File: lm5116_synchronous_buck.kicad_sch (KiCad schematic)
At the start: 60 parts

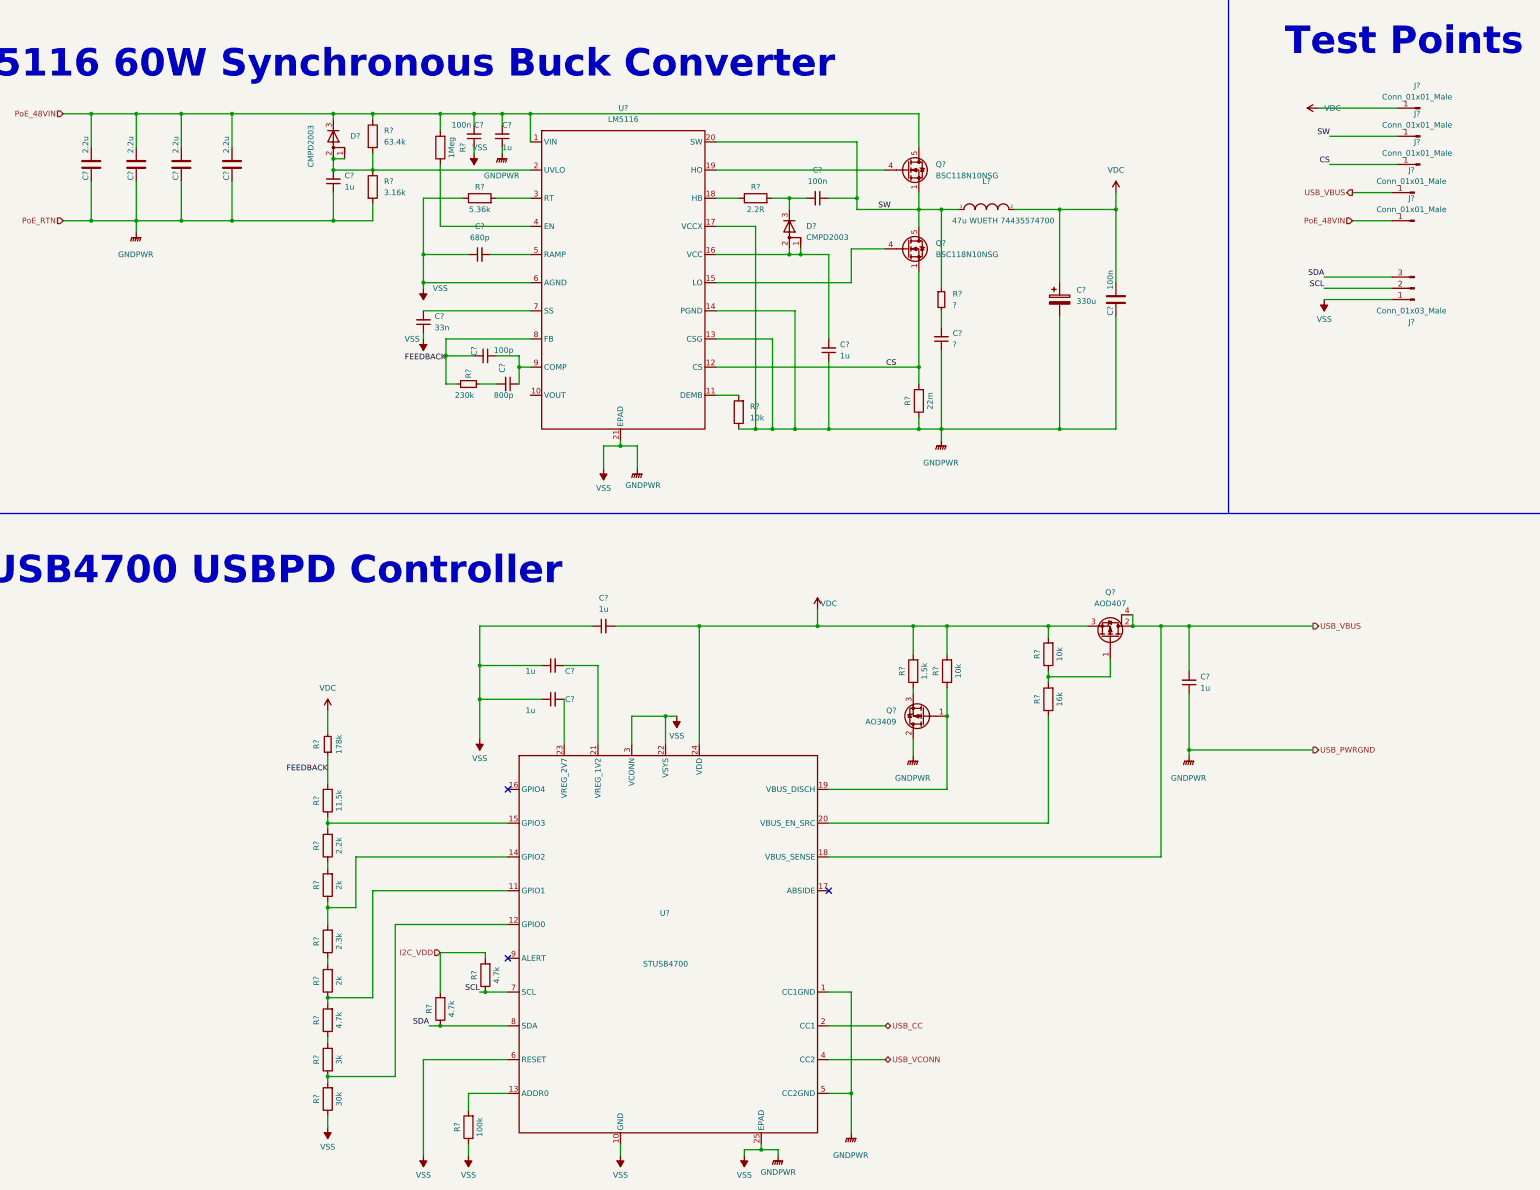
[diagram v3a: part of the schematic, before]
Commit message: finished lm5116 circuit foot print assignment
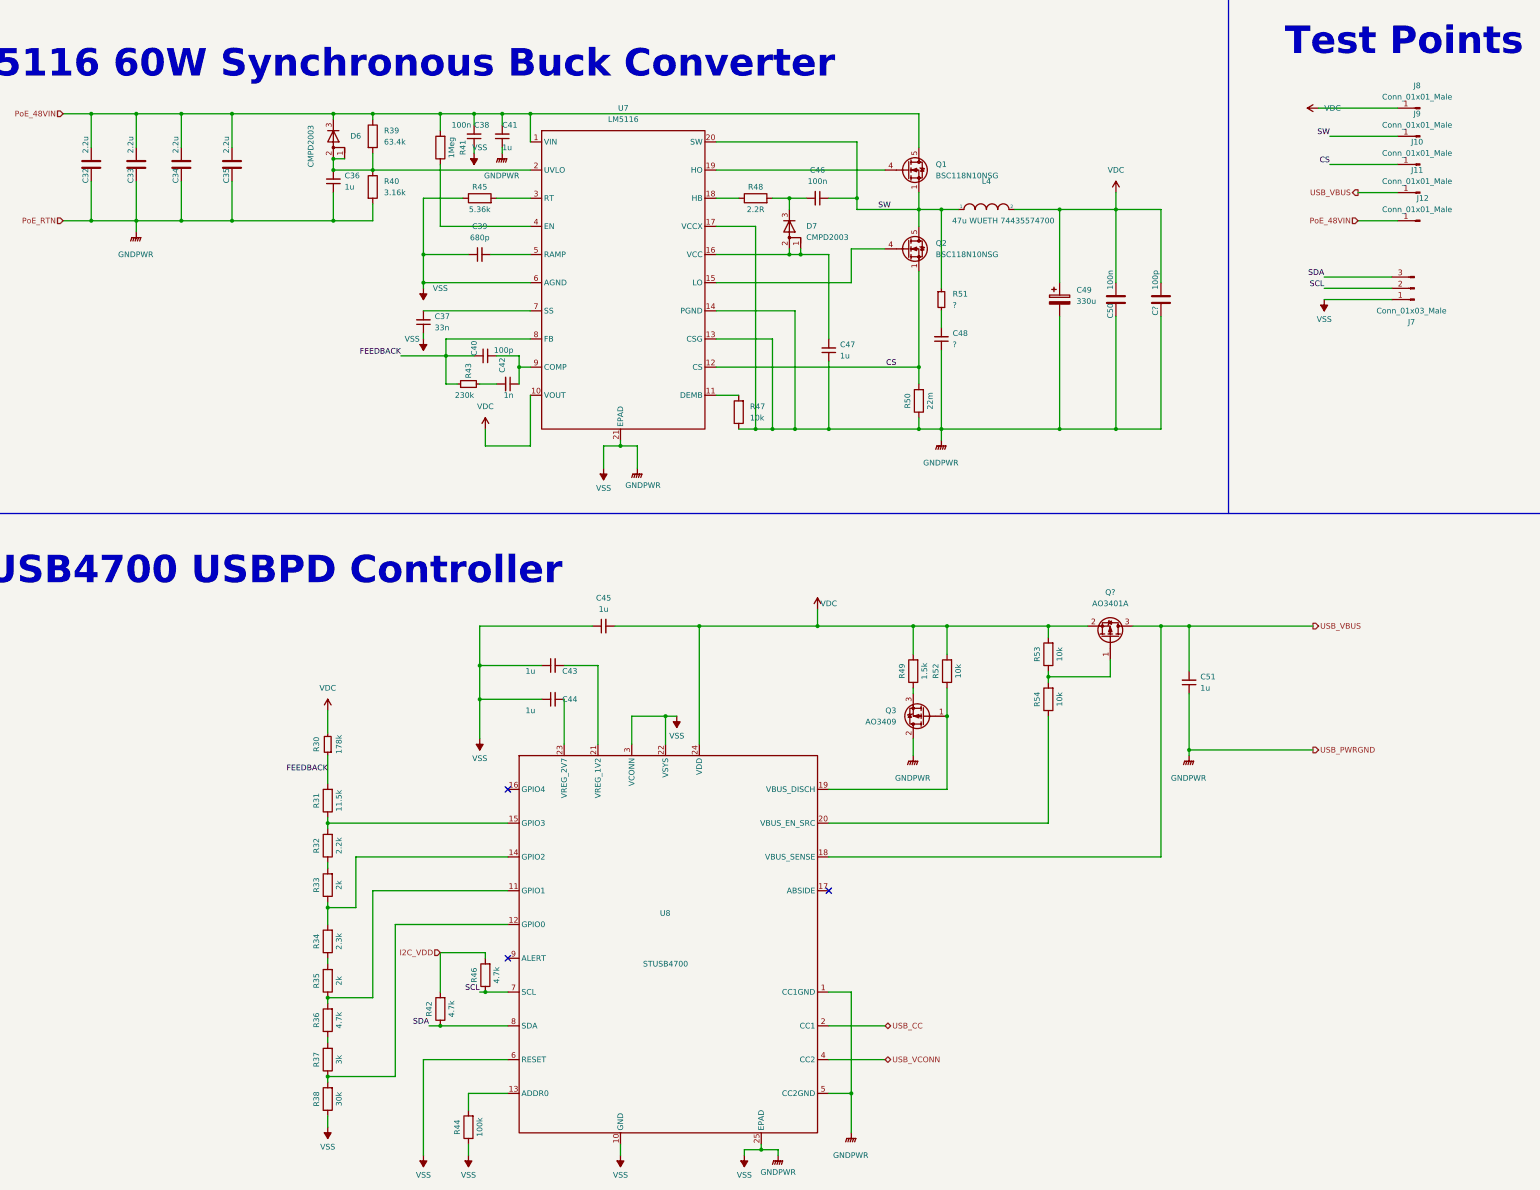
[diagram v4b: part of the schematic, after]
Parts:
- removed Q?: AOD407, symbol Device:Q_PMOS_GDSD
- added C?: 100p, Capacitor_SMD:C_0603_1608Metric, symbol Device:C
- added Q?: AO3401A, Package_TO_SOT_SMD:SOT-23, symbol Transistor_FET:AO3401A
- C32, C33, C34, C35, C36, C37, C38, C39, C40, C41, C43, C44, C45, C46, C47, C48, C50: renamed from C?; footprint (none) -> Capacitor_SMD:C_0603_1608Metric
- C42: renamed from C?; value 800p -> 1n; footprint (none) -> Capacitor_SMD:C_0603_1608Metric
- D6, D7: renamed from D?; footprint (none) -> Package_TO_SOT_SMD:SOT-23
- J10, J11, J12, J8, J9: renamed from J?; footprint (none) -> Connector_PinHeader_1.00mm:PinHeader_1x01_P1.00mm_Vertical
- J7: renamed from J?; footprint (none) -> Connector_PinHeader_1.00mm:PinHeader_1x03_P1.00mm_Vertical
- Q3: renamed from Q?; footprint (none) -> Package_TO_SOT_SMD:SOT-23
- R30, R31, R32, R33, R34, R35, R36, R37, R38, R40, R41, R42, R43, R44, R45, R46, R47, R49, R51, R52, R53: renamed from R?; footprint (none) -> Resistor_SMD:R_0603_1608Metric
- R48: renamed from R?; footprint (none) -> Resistor_SMD:R_0805_2012Metric
- R50: renamed from R?; footprint (none) -> Resistor_SMD:R_1206_3216Metric
- R54: renamed from R?; value 16k -> 10k; footprint (none) -> Resistor_SMD:R_0603_1608Metric
- gave numbers to parts that had none: 8
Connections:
- net GNDPWR: now also C?.2
- net USB_VBUS: now also Q?.3 (D)
- net VDC: now also U7.10 (VOUT), C?.1, Q?.2 (S)
- net at R53.1, R54.2: now also Q?.1 (G)
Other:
- moved on the sheet: J11, J12

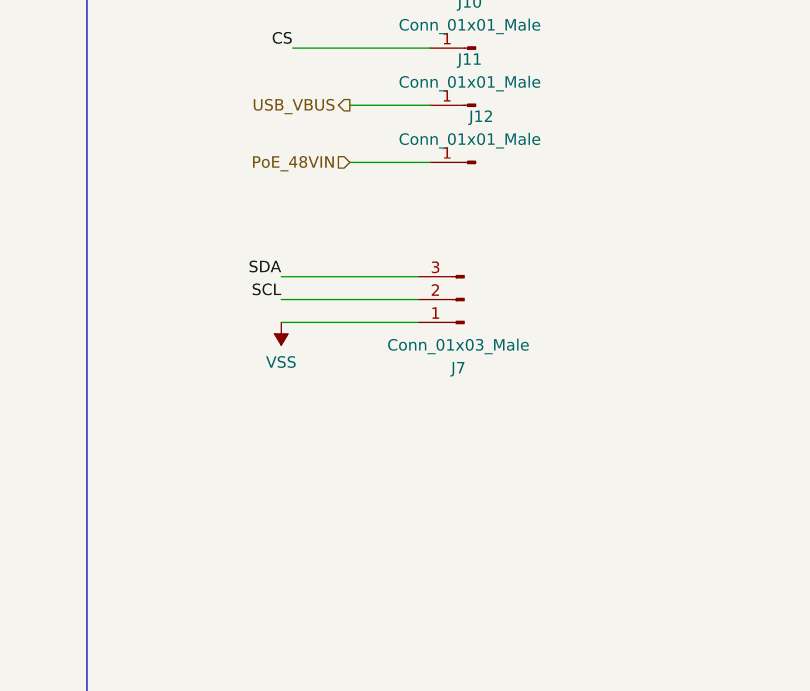
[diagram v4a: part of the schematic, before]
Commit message: footprint for power inductor and cap
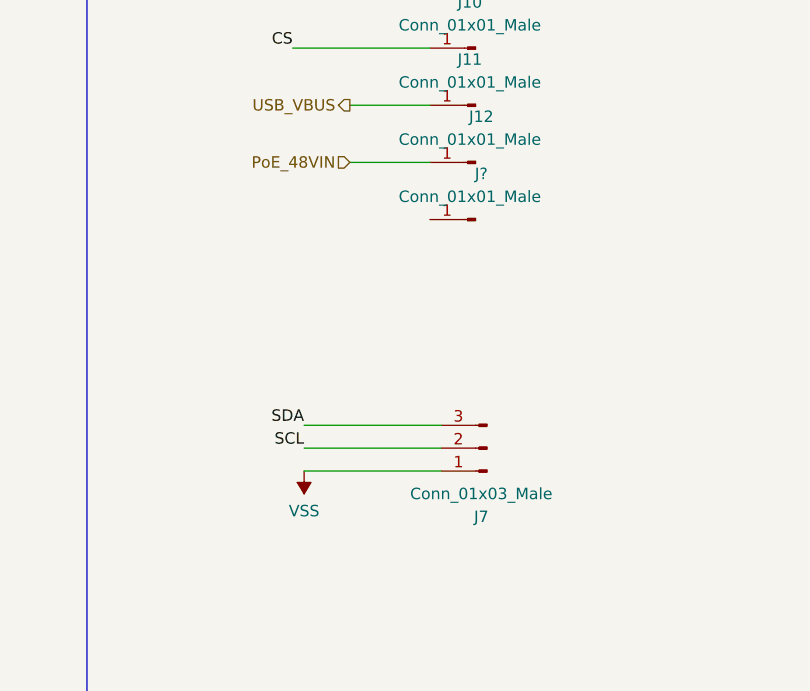
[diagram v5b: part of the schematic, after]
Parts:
- added J?: Conn_01x01_Male, Connector_PinHeader_1.00mm:PinHeader_1x01_P1.00mm_Vertical, symbol Connector:Conn_01x01_Male
- C49: footprint (none) -> Capacitor_SMD:C_Elec_10x10.2
- L4: footprint (none) -> PoE_Devices:74435574700
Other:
- moved on the sheet: J7
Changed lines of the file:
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@@
     (stroke (width 0) (type default) (color 0 0 0 0))
   )
-  (wire (pts (xy 331.47 82.55) (xy 346.71 82.55))
+  (wire (pts (xy 334.01 99.06) (xy 349.25 99.06))
     (stroke (width 0) (type default) (color 0 0 0 0))
   )
@@
     (stroke (width 0) (type default) (color 0 0 0 0))
   )
-  (wire (pts (xy 331.47 80.01) (xy 346.71 80.01))
+  (wire (pts (xy 334.01 96.52) (xy 349.25 96.52))
     (stroke (width 0) (type default) (color 0 0 0 0))
   )
@@
     (stroke (width 0) (type default) (color 0 0 0 0))
   )
-  (wire (pts (xy 331.47 77.47) (xy 346.71 77.47))
+  (wire (pts (xy 334.01 93.98) (xy 349.25 93.98))
     (stroke (width 0) (type default) (color 0 0 0 0))
   )
@@
     (effects (font (size 6.2 6.2) (thickness 1.4) bold) (justify left bottom))
   )
-  (label "SDA" (at 331.47 77.47 180)
+  (label "SDA" (at 334.01 93.98 180)
     (effects (font (size 1.27 1.27)) (justify right bottom))
   )
@@
     (effects (font (size 1.27 1.27)) (justify right bottom))
   )
-  (label "SCL" (at 331.47 80.01 180)
+  (label "SCL" (at 334.01 96.52 180)
     (effects (font (size 1.27 1.27)) (justify right bottom))
   )
@@
     (property "Reference" "L4" (id 0) (at 255.27 55.88 0))
     (property "Value" "47u WUETH 74435574700 " (id 1) (at 259.08 64.77 0))
-    (property "Footprint" "" (id 2) (at 255.27 62.23 0)
+    (property "Footprint" "PoE_Devices:74435574700" (id 2) (at 255.27 62.23 0)
       (effects (font (size 1.27 1.27)) hide)
     )
@@
       (effects (font (size 1.27 1.27)) (justify left))
     )
-    (property "Footprint" "" (id 2) (at 272.7452 86.36 0)
+    (property "Footprint" "Capacitor_SMD:C_Elec_10x10.2" (id 2) (at 272.7452 86.36 0)
       (effects (font (size 1.27 1.27)) hide)
     )
@@
     (pin "2")
   )
-  (symbol (lib_id "Connector:Conn_01x03_Male") (at 351.79 80.01 180) (unit 1)
-    (in_bom yes) (on_board yes) (fields_autoplaced)
-    (property "Reference" "J7" (id 0) (at 351.155 87.63 0))
-    (property "Value" "Conn_01x03_Male" (id 1) (at 351.155 85.09 0))
-    (property "Footprint" "Connector_PinHeader_1.00mm:PinHeader_1x03_P1.00mm_Vertical" (id 2) (at 351.79 80.01 0)
-      (effects (font (size 1.27 1.27)) hide)
-    )
-    (property "Datasheet" "~" (id 3) (at 351.79 80.01 0)
+  (symbol (lib_id "Connector:Conn_01x03_Male") (at 354.33 96.52 180) (unit 1)
+    (in_bom yes) (on_board yes) (fields_autoplaced)
+    (property "Reference" "J7" (id 0) (at 353.695 104.14 0))
+    (property "Value" "Conn_01x03_Male" (id 1) (at 353.695 101.6 0))
+    (property "Footprint" "Connector_PinHeader_1.00mm:PinHeader_1x03_P1.00mm_Vertical" (id 2) (at 354.33 96.52 0)
+      (effects (font (size 1.27 1.27)) hide)
+    )
+    (property "Datasheet" "~" (id 3) (at 354.33 96.52 0)
       (effects (font (size 1.27 1.27)) hide)
     )
@@
     (pin "2")
   )
-  (symbol (lib_id "power:VSS") (at 331.47 82.55 180) (unit 1)
-    (in_bom yes) (on_board yes) (fields_autoplaced)
-    (property "Reference" "#PWR039" (id 0) (at 331.47 78.74 0)
-      (effects (font (size 1.27 1.27)) hide)
-    )
-    (property "Value" "VSS" (id 1) (at 331.47 86.995 0))
-    (property "Footprint" "" (id 2) (at 331.47 82.55 0)
-      (effects (font (size 1.27 1.27)) hide)
-    )
-    (property "Datasheet" "" (id 3) (at 331.47 82.55 0)
+  (symbol (lib_id "power:VSS") (at 334.01 99.06 180) (unit 1)
+    (in_bom yes) (on_board yes) (fields_autoplaced)
+    (property "Reference" "#PWR039" (id 0) (at 334.01 95.25 0)
+      (effects (font (size 1.27 1.27)) hide)
+    )
+    (property "Value" "VSS" (id 1) (at 334.01 103.505 0))
+    (property "Footprint" "" (id 2) (at 334.01 99.06 0)
+      (effects (font (size 1.27 1.27)) hide)
+    )
+    (property "Datasheet" "" (id 3) (at 334.01 99.06 0)
       (effects (font (size 1.27 1.27)) hide)
     )
@@
     (pin "2")
   )
+  (symbol (lib_id "Connector:Conn_01x01_Male") (at 353.06 71.12 180) (unit 1)
+    (in_bom yes) (on_board yes)
+    (property "Reference" "J?" (id 0) (at 353.695 66.04 0))
+    (property "Value" "Conn_01x01_Male" (id 1) (at 352.425 68.58 0))
+    (property "Footprint" "Connector_PinHeader_1.00mm:PinHeader_1x01_P1.00mm_Vertical" (id 2) (at 353.06 71.12 0)
+      (effects (font (size 1.27 1.27)) hide)
+    )
+    (property "Datasheet" "~" (id 3) (at 353.06 71.12 0)
+      (effects (font (size 1.27 1.27)) hide)
+    )
+    (pin "1")
+  )
   (symbol (lib_id "Device:Q_PMOS_GDS") (at 241.3 176.53 180) (unit 1)

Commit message: footprint update
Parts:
- added C?: 1u, symbol Device:C_Small
- added Q?: AO3401A, Package_TO_SOT_SMD:SOT-23, symbol Transistor_FET:AO3401A
- added R?: 10k, Resistor_SMD:R_0603_1608Metric, symbol Device:R
- C48, R51: now left out of the parts list
- C51: value 1u -> 10u
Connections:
- net GNDPWR: now also R49.1, C?.1; no longer Q3.2 (D)
- net USB_VBUS: now also C?.2
- net VDC: now also Q3.3 (S), Q?.3 (D); no longer Q?.2 (S), R49.2, R53.2
- net ABSIDE: now reaches U8.17 (ABSIDE)
- net ABSIDE: now also J?.1 (Pin_1)
- net at Q3.1 (G), R52.1: now also R?.2; no longer U8.19 (VBUS_DISCH)
- net at Q?.1 (G), R53.1, R54.2: now also Q?.1 (G)
- new net: R?.1, U8.19 (VBUS_DISCH)
- new net: Q3.2 (D), R49.2
- new net: Q?.2 (S), Q?.2 (S), R53.2
- no-connect marks 3 -> 2
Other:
- moved on the sheet: Q3, R49, R52

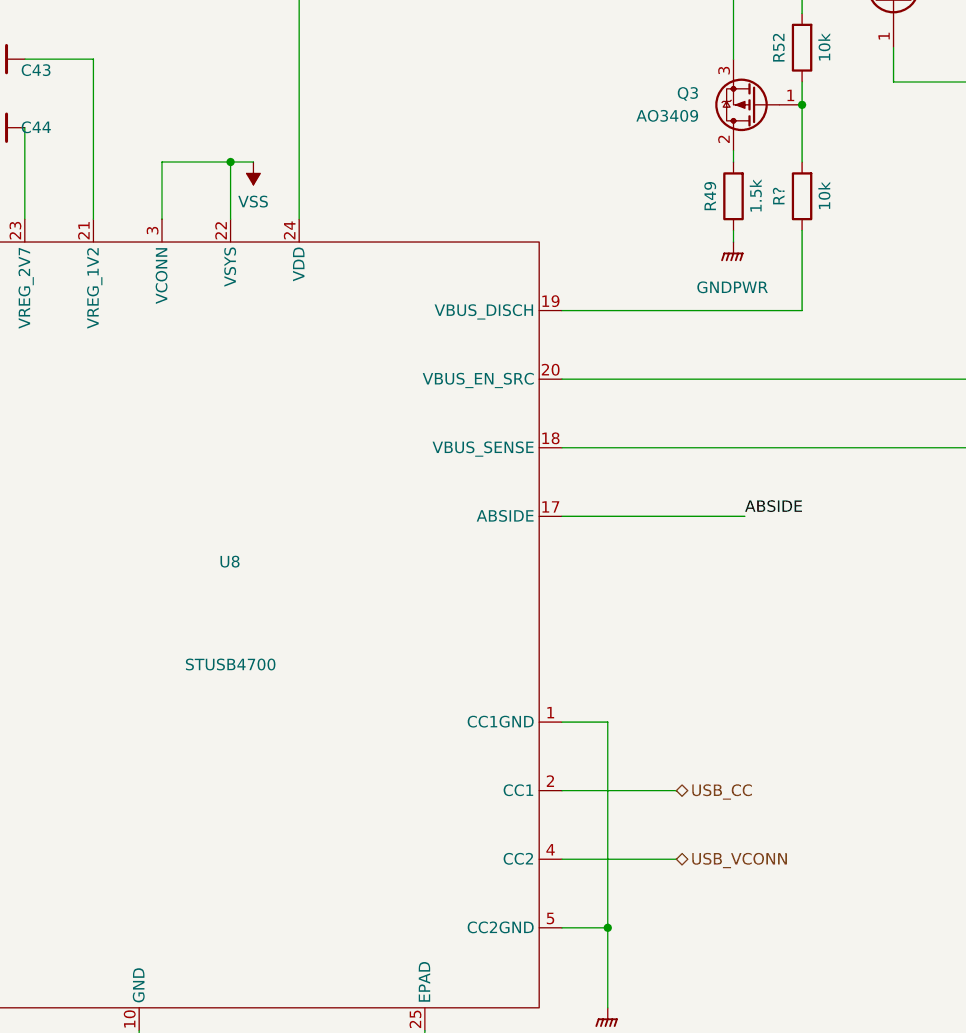
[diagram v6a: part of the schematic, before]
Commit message: changed CC pin tags
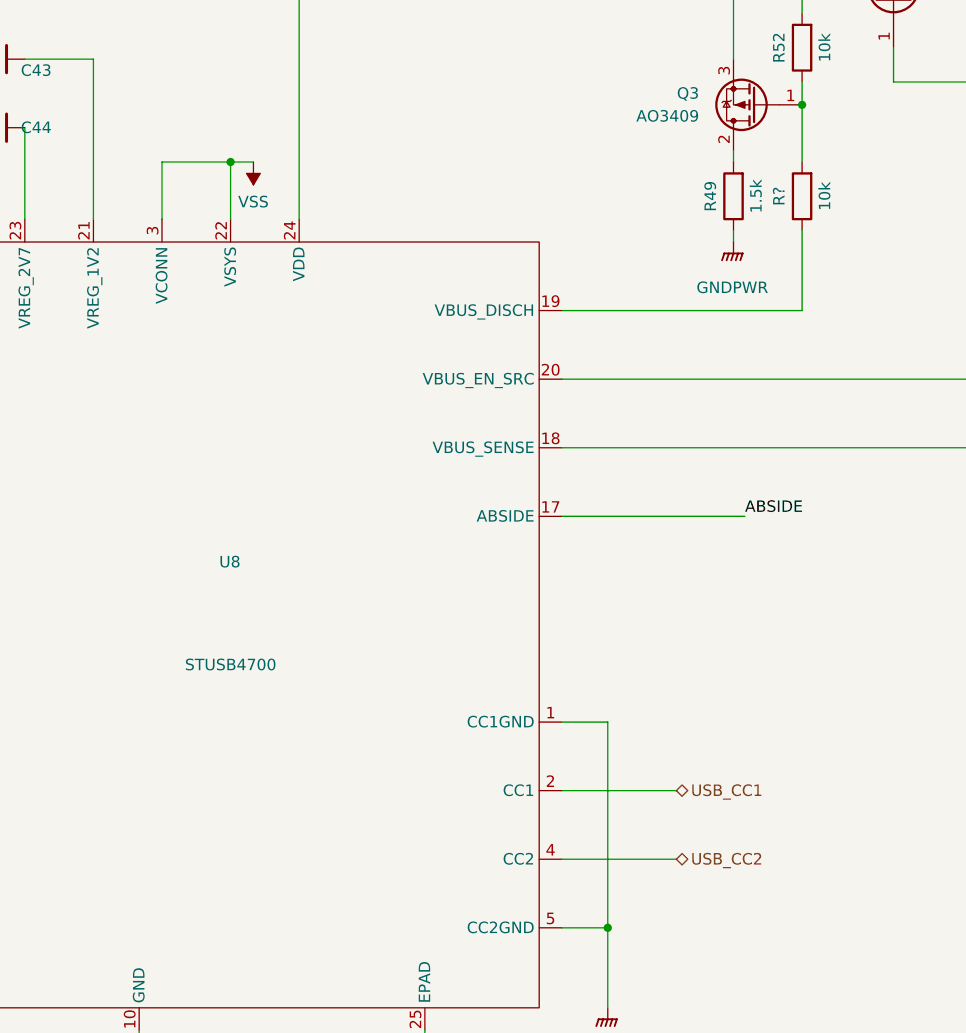
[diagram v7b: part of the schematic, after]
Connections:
- net USB_CC renamed USB_CC1
- net USB_VCONN renamed USB_CC2
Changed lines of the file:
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@@
   (junction (at 63.5 64.77) (diameter 0) (color 0 0 0 0)
   )
+  (junction (at 182.88 176.53) (diameter 0) (color 0 0 0 0)
+  )
   (junction (at 172.72 115.57) (diameter 0) (color 0 0 0 0)
   )
@@
   )
   (junction (at 63.5 40.64) (diameter 0) (color 0 0 0 0)
-  )
-  (junction (at 182.88 176.53) (diameter 0) (color 0 0 0 0)
   )
   (junction (at 312.42 156.21) (diameter 0) (color 0 0 0 0)
@@
     (stroke (width 0) (type default) (color 0 0 0 0))
   )
-  (wire (pts (xy 182.88 176.53) (xy 175.26 176.53))
-    (stroke (width 0) (type default) (color 0 0 0 0))
-  )
   (wire (pts (xy 142.24 238.76) (xy 147.32 238.76))
     (stroke (width 0) (type default) (color 0 0 0 0))
@@
     (stroke (width 0) (type default) (color 0 0 0 0))
   )
+  (wire (pts (xy 175.26 182.88) (xy 175.26 176.53))
+    (stroke (width 0) (type default) (color 0 0 0 0))
+  )
   (wire (pts (xy 256.54 163.83) (xy 256.54 167.64))
     (stroke (width 0) (type default) (color 0 0 0 0))
@@
     (stroke (width 0) (type default) (color 0 0 0 0))
   )
+  (wire (pts (xy 175.26 176.53) (xy 182.88 176.53))
+    (stroke (width 0) (type default) (color 0 0 0 0))
+  )
   (wire (pts (xy 139.7 40.64) (xy 146.05 40.64))
     (stroke (width 0) (type default) (color 0 0 0 0))
@@
   )
   (wire (pts (xy 300.99 171.45) (xy 300.99 184.15))
-    (stroke (width 0) (type default) (color 0 0 0 0))
-  )
-  (wire (pts (xy 175.26 176.53) (xy 175.26 182.88))
     (stroke (width 0) (type default) (color 0 0 0 0))
   )
@@
     (effects (font (size 1.27 1.27)) (justify right))
   )
-  (hierarchical_label "USB_CC" (shape bidirectional) (at 232.41 246.38 0)
+  (hierarchical_label "USB_CC1" (shape bidirectional) (at 232.41 246.38 0)
     (effects (font (size 1.27 1.27)) (justify left))
   )
-  (hierarchical_label "USB_VCONN" (shape bidirectional) (at 232.41 254 0)
+  (hierarchical_label "USB_CC2" (shape bidirectional) (at 232.41 254 0)
     (effects (font (size 1.27 1.27)) (justify left))
   )
